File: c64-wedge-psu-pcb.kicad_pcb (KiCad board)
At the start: 2 copper layers, 70 x 54 mm, 16 parts, among them U1 LM2576T-5

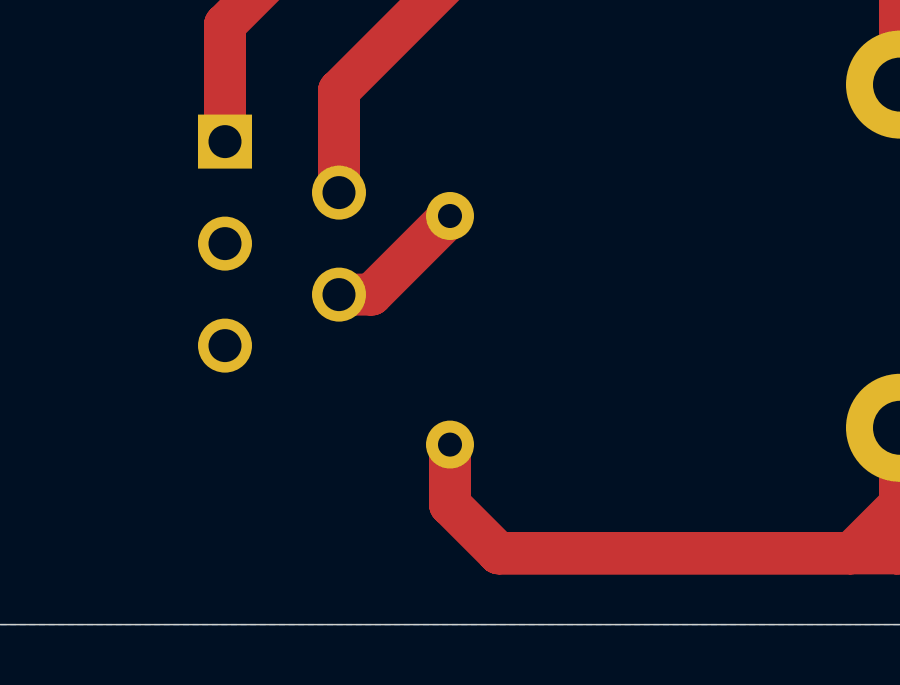
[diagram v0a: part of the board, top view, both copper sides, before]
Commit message: Make R1 pads bigger
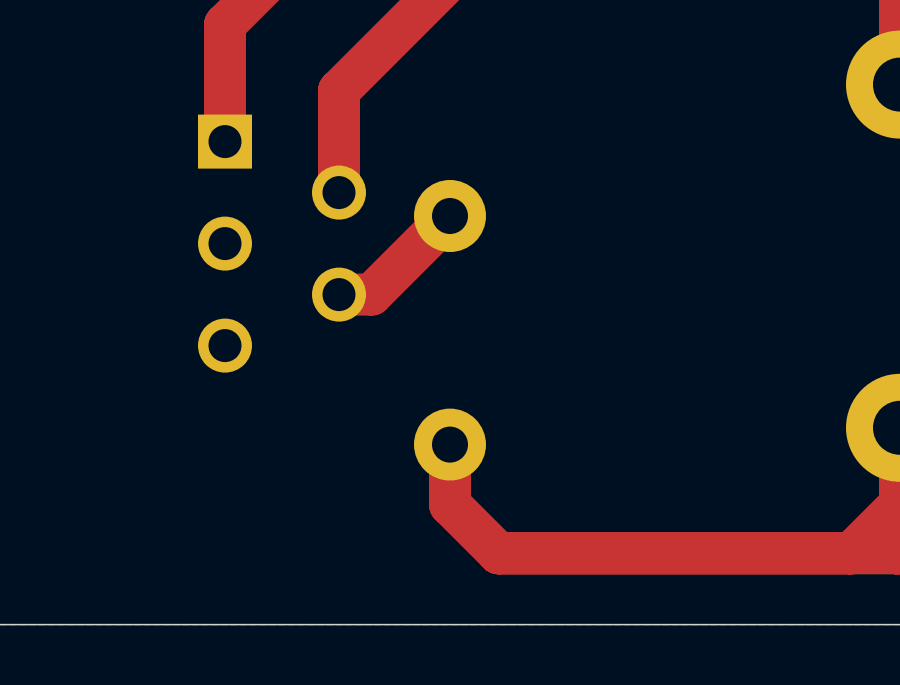
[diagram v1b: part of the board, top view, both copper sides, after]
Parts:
- R1: footprint Resistor_THT:R_Axial_DIN0207_L6.3mm_D2.5mm_P7.62mm_Horizontal -> Resistor_THT:R_Axial_DIN0411_L9.9mm_D3.6mm_P7.62mm_Vertical
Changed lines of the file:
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@@
     (add_net "Net-(R1-Pad2)")
+  )
+  (module Resistor_THT:R_Axial_DIN0411_L9.9mm_D3.6mm_P7.62mm_Vertical (layer B.Cu)
+    (at 117.5 108 90)
+    (descr "Resistor, Axial_DIN0411 series, Axial, Vertical, pin pitch=7.62mm, 1W, length*diameter=9.9*3.6mm^2")
+    (tags "Resistor Axial_DIN0411 series Axial Vertical pin pitch 7.62mm 1W length 9.9mm diameter 3.6mm")
+    (fp_text reference R1 (at 4 0 180) (layer B.SilkS)
+      (effects (font (size 1 1) (thickness 0.15)) (justify mirror))
+    )
+    (fp_text value 0R (at 3.81 -2.92 90) (layer B.Fab)
+      (effects (font (size 1 1) (thickness 0.15)) (justify mirror))
+    )
+    (fp_text user %R (at 3.81 2.92 90) (layer B.Fab)
+      (effects (font (size 1 1) (thickness 0.15)) (justify mirror))
+    )
+    (fp_line (start 9.07 2.05) (end -2.05 2.05) (layer B.CrtYd) (width 0.05))
+    (fp_line (start 9.07 -2.05) (end 9.07 2.05) (layer B.CrtYd) (width 0.05))
+    (fp_line (start -2.05 -2.05) (end 9.07 -2.05) (layer B.CrtYd) (width 0.05))
+    (fp_line (start -2.05 2.05) (end -2.05 -2.05) (layer B.CrtYd) (width 0.05))
+    (fp_line (start 1.92 0) (end 6.12 0) (layer B.SilkS) (width 0.12))
+    (fp_line (start 0 0) (end 7.62 0) (layer B.Fab) (width 0.1))
+    (fp_circle (center 0 0) (end 1.92 0) (layer B.SilkS) (width 0.12))
+    (fp_circle (center 0 0) (end 1.8 0) (layer B.Fab) (width 0.1))
+    (pad 2 thru_hole oval (at 7.62 0 90) (size 2.4 2.4) (drill 1.2) (layers *.Cu *.Mask)
+      (net 8 "Net-(R1-Pad2)"))
+    (pad 1 thru_hole circle (at 0 0 90) (size 2.4 2.4) (drill 1.2) (layers *.Cu *.Mask)
+      (net 2 "Net-(C2-Pad1)"))
+    (model ${KISYS3DMOD}/Resistor_THT.3dshapes/R_Axial_DIN0411_L9.9mm_D3.6mm_P7.62mm_Vertical.wrl
+      (at (xyz 0 0 0))
+      (scale (xyz 1 1 1))
+      (rotate (xyz 0 0 0))
+    )
   )
   (module Symbol:OSHW-Logo2_7.3x6mm_SilkScreen (layer F.Cu)
@@
       (effects (font (size 1 1) (thickness 0.15)) (justify mirror))
     )
-    (fp_text user K (at 0 2.6 90) (layer B.SilkS)
+    (fp_text user K (at 0 2.6 180) (layer B.SilkS)
       (effects (font (size 1 1) (thickness 0.15)) (justify mirror))
     )
@@
     )
   )
-  (module Resistor_THT:R_Axial_DIN0207_L6.3mm_D2.5mm_P7.62mm_Horizontal (layer B.Cu)
-    (at 117.5 108 90)
-    (descr "Resistor, Axial_DIN0207 series, Axial, Horizontal, pin pitch=7.62mm, 0.25W = 1/4W, length*diameter=6.3*2.5mm^2, http://cdn-reichelt.de/documents/datenblatt/B400/1_4W%23YAG.pdf")
-    (tags "Resistor Axial_DIN0207 series Axial Horizontal pin pitch 7.62mm 0.25W = 1/4W length 6.3mm diameter 2.5mm")
-    (fp_text reference R1 (at 3.81 0 180) (layer B.SilkS)
-      (effects (font (size 1 1) (thickness 0.15)) (justify mirror))
-    )
-    (fp_text value 0R (at 3.81 -2.37 90) (layer B.Fab)
-      (effects (font (size 1 1) (thickness 0.15)) (justify mirror))
-    )
-    (fp_line (start 0.66 1.25) (end 0.66 -1.25) (layer B.Fab) (width 0.1))
-    (fp_line (start 0.66 -1.25) (end 6.96 -1.25) (layer B.Fab) (width 0.1))
-    (fp_line (start 6.96 -1.25) (end 6.96 1.25) (layer B.Fab) (width 0.1))
-    (fp_line (start 6.96 1.25) (end 0.66 1.25) (layer B.Fab) (width 0.1))
-    (fp_line (start 0 0) (end 0.66 0) (layer B.Fab) (width 0.1))
-    (fp_line (start 7.62 0) (end 6.96 0) (layer B.Fab) (width 0.1))
-    (fp_line (start 0.54 1.04) (end 0.54 1.37) (layer B.SilkS) (width 0.12))
-    (fp_line (start 0.54 1.37) (end 7.08 1.37) (layer B.SilkS) (width 0.12))
-    (fp_line (start 7.08 1.37) (end 7.08 1.04) (layer B.SilkS) (width 0.12))
-    (fp_line (start 0.54 -1.04) (end 0.54 -1.37) (layer B.SilkS) (width 0.12))
-    (fp_line (start 0.54 -1.37) (end 7.08 -1.37) (layer B.SilkS) (width 0.12))
-    (fp_line (start 7.08 -1.37) (end 7.08 -1.04) (layer B.SilkS) (width 0.12))
-    (fp_line (start -1.05 1.5) (end -1.05 -1.5) (layer B.CrtYd) (width 0.05))
-    (fp_line (start -1.05 -1.5) (end 8.67 -1.5) (layer B.CrtYd) (width 0.05))
-    (fp_line (start 8.67 -1.5) (end 8.67 1.5) (layer B.CrtYd) (width 0.05))
-    (fp_line (start 8.67 1.5) (end -1.05 1.5) (layer B.CrtYd) (width 0.05))
-    (fp_text user %R (at 3.81 0 90) (layer B.Fab)
-      (effects (font (size 1 1) (thickness 0.15)) (justify mirror))
-    )
-    (pad 1 thru_hole circle (at 0 0 90) (size 1.6 1.6) (drill 0.8) (layers *.Cu *.Mask)
-      (net 2 "Net-(C2-Pad1)"))
-    (pad 2 thru_hole oval (at 7.62 0 90) (size 1.6 1.6) (drill 0.8) (layers *.Cu *.Mask)
-      (net 8 "Net-(R1-Pad2)"))
-    (model ${KISYS3DMOD}/Resistor_THT.3dshapes/R_Axial_DIN0207_L6.3mm_D2.5mm_P7.62mm_Horizontal.wrl
-      (at (xyz 0 0 0))
-      (scale (xyz 1 1 1))
-      (rotate (xyz 0 0 0))
-    )
-  )
   (module Connector_PinHeader_2.54mm:PinHeader_1x02_P2.54mm_Vertical (layer B.Cu)
     (at 152 80.5 270)
@@
   (segment (start 146 111) (end 145.37501 111.62499) (width 1.4) (layer F.Cu) (net 2))
   (segment (start 141 88) (end 146 93) (width 1.4) (layer F.Cu) (net 2))
-  (segment (start 117.5 110) (end 117.5 108) (width 1.4) (layer F.Cu) (net 2))
   (segment (start 130.860594 111.62499) (end 119.12499 111.62499) (width 1.4) (layer F.Cu) (net 2))
   (segment (start 132.5 107.44) (end 132.5 109.985584) (width 1.4) (layer F.Cu) (net 2))
@@
   (segment (start 146 100) (end 146 102) (width 1.4) (layer F.Cu) (net 2))
   (segment (start 146 102) (end 146 111) (width 1.4) (layer F.Cu) (net 2))
+  (segment (start 117.5 108) (end 117.5 110) (width 1.4) (layer F.Cu) (net 2))
   (segment (start 93.5 73.5) (end 93.5 77.6) (width 1.4) (layer F.Cu) (net 3))
   (segment (start 104 63) (end 93.5 73.5) (width 1.4) (layer F.Cu) (net 3))
@@
   (segment (start 142 63) (end 149 70) (width 1.4) (layer F.Cu) (net 7))
   (segment (start 149 70) (end 152 70) (width 1.4) (layer F.Cu) (net 7))
+  (segment (start 113.8 103) (end 114.88 103) (width 1.4) (layer F.Cu) (net 8))
   (segment (start 114.88 103) (end 117.5 100.38) (width 1.4) (layer F.Cu) (net 8))
-  (segment (start 113.8 103) (end 114.88 103) (width 1.4) (layer F.Cu) (net 8))
   (segment (start 152 79.12) (end 149.38 76.5) (width 1.4) (layer F.Cu) (net 9))
   (segment (start 152 80.5) (end 152 79.12) (width 1.4) (layer F.Cu) (net 9))

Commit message: relayout, change some values and footprints
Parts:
- C1, C2: footprint Capacitor_THT:CP_Radial_D18.0mm_P7.50mm -> Capacitor_THT:CP_Radial_D16.0mm_P7.50mm
- C3: footprint Capacitor_THT:CP_Radial_D6.3mm_P2.50mm -> Capacitor_THT:CP_Radial_D8.0mm_P3.50mm
- L2: renamed from L3; value 22uH -> 20uH; footprint Inductor_THT:L_Toroid_Vertical_L19.1mm_W8.1mm_P7.10mm_Bourns_5700 -> Inductor_THT:L_Toroid_Vertical_L16.0mm_W8.0mm_P7.62mm
- R1: footprint Resistor_THT:R_Axial_DIN0411_L9.9mm_D3.6mm_P7.62mm_Vertical -> Resistor_THT:R_Axial_DIN0411_L9.9mm_D3.6mm_P5.08mm_Vertical
- U1: footprint Package_TO_SOT_THT:TO-220-5_P3.4x3.8mm_StaggerEven_Lead7.13mm_TabDown -> Package_TO_SOT_THT:TO-220-5_P3.4x3.7mm_StaggerEven_Lead3.8mm_Vertical
- moved R1 15.3 mm to (132.5, 111.0), turned to 180 degrees
- moved U1 2.56 mm to (112.5, 97.3)
- moved C1 1.12 mm to (115.5, 87.0)
- moved C2 1.00 mm to (141.0, 87.0)
- moved L1 1.00 mm to (132.5, 95.0)
- moved C3 0.90 mm to (156.5, 86.8)
- moved D2 0.50 mm to (128.5, 89.5)
- moved L2 0.50 mm to (148.5, 101.0)
- renumbered L2 to L1
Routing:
- net Net-(C2-Pad1): track 92.8 -> 52.5 mm
- net Net-(R1-Pad2): track 4.79 -> 18.1 mm
- net Net-(D2-Pad1): track 29.2 -> 27.1 mm

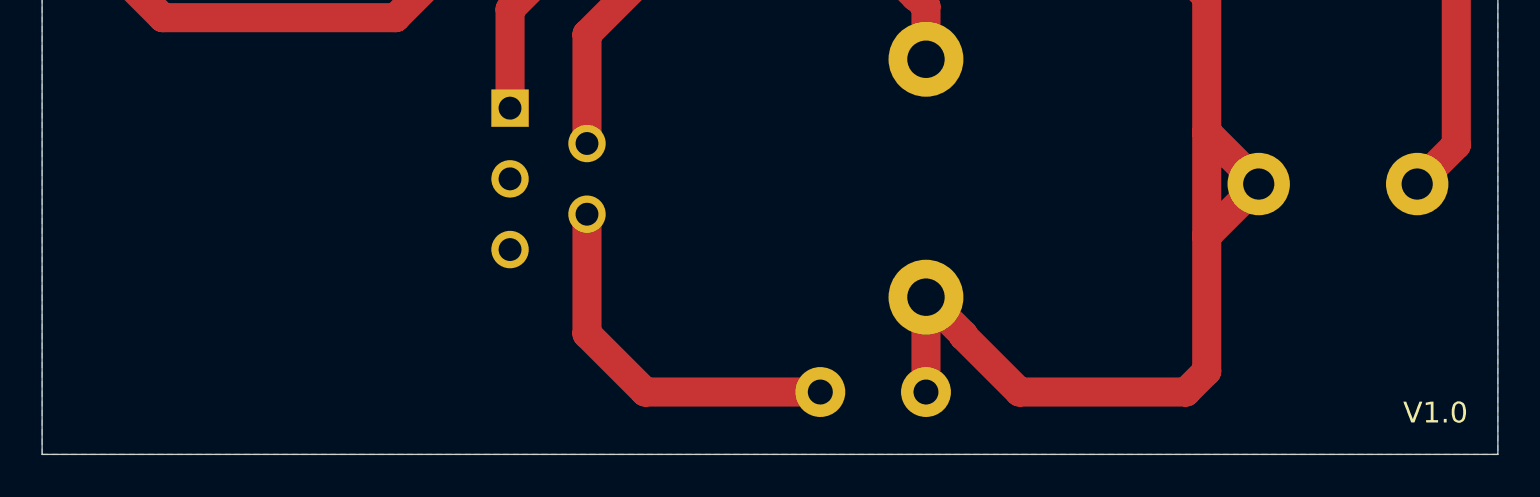
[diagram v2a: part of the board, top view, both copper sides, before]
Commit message: Modify footprints, add some info text, modify resistor values
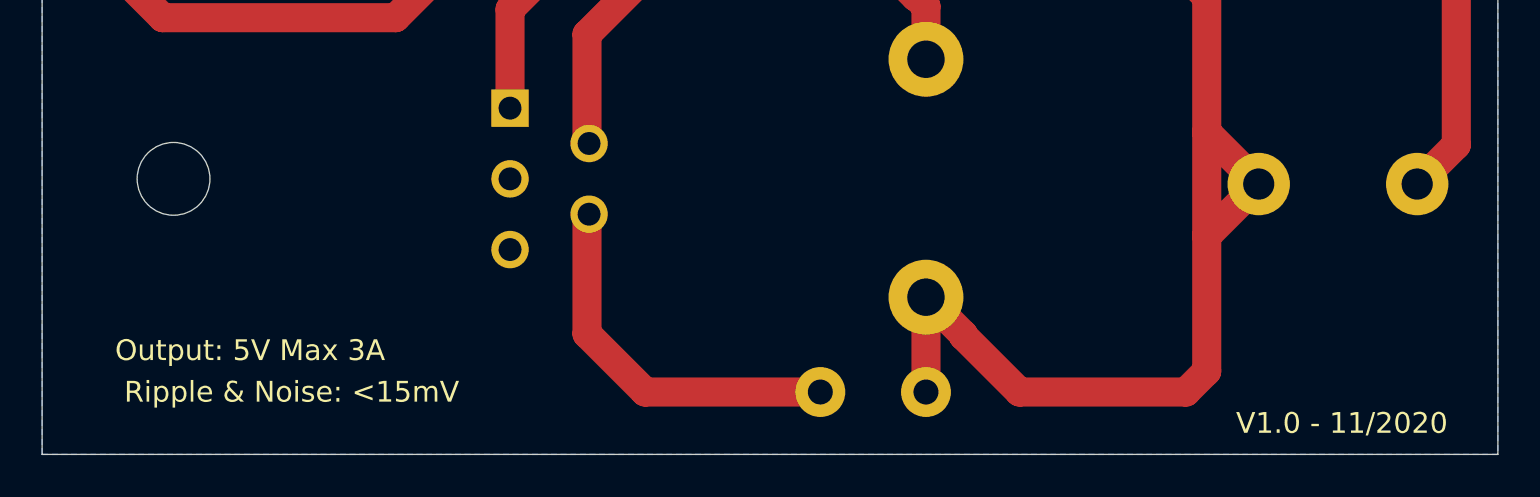
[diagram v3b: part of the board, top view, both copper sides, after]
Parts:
- C3: value 100uF -> 220uF 50V
- R1: value 0R -> 200R
- R2: value 330R -> 200R
- U1: footprint Package_TO_SOT_THT:TO-220-5_P3.4x3.7mm_StaggerEven_Lead3.8mm_Vertical -> Package_TO_SOT_THT:TO-220-5_P3.4x3.8mm_StaggerEven_Lead7.13mm_TabDown
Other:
- board text added: "Output: 5V Max 3A"
- board text added: "Ripple & Noise: <15mV"
- board text added: "V1.0 - 11/2020"
- board text removed: "V1.0"

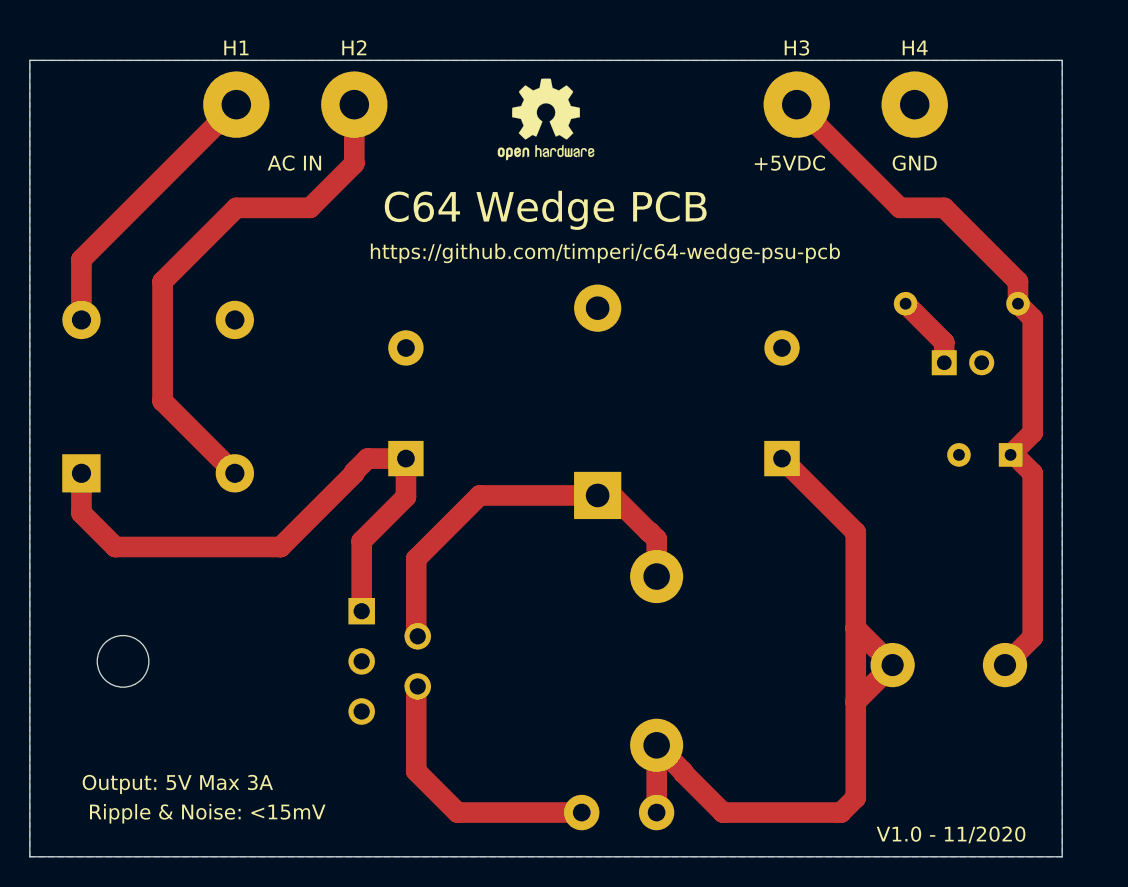
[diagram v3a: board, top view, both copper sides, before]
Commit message: V1.1: Proper voltage divider to Feedback line. Make tracks wider. Some relayout. Update resistor values and L2 value.
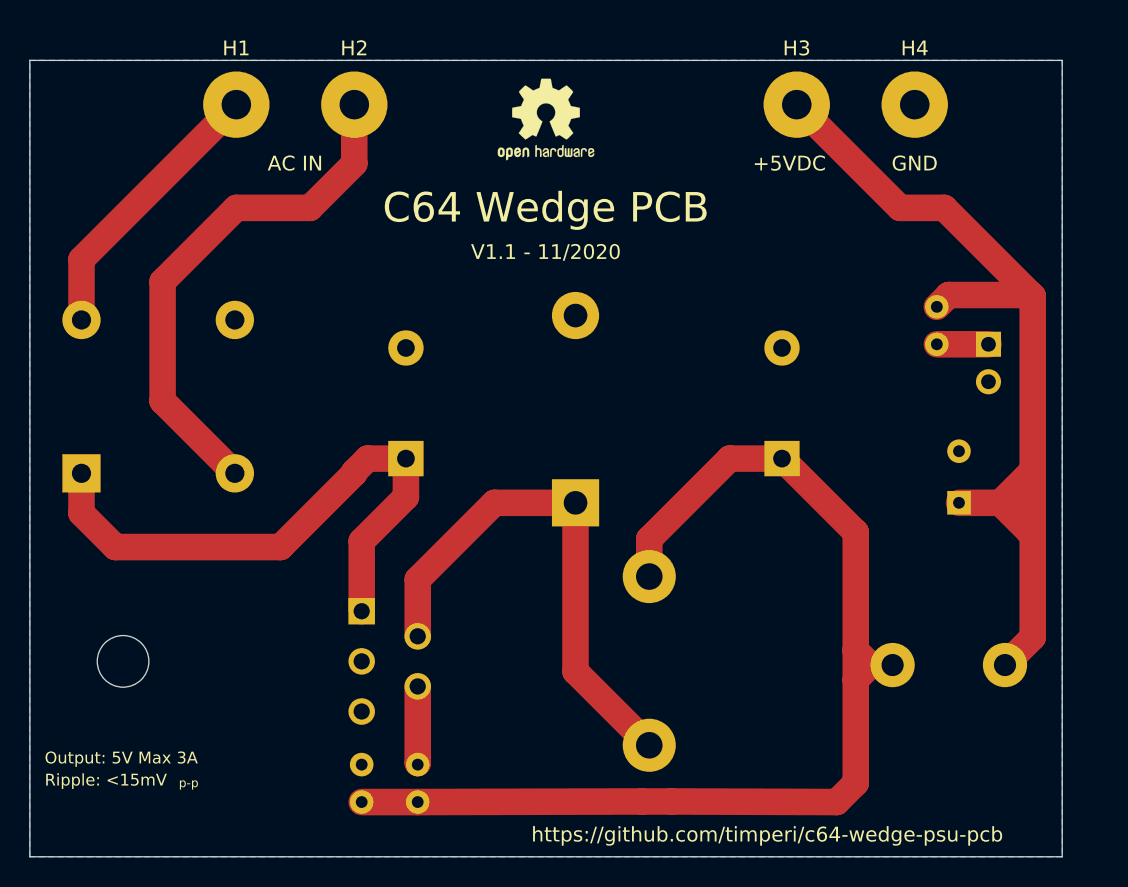
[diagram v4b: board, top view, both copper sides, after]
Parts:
- added R3: 5000R, Resistor_THT:R_Axial_DIN0207_L6.3mm_D2.5mm_P2.54mm_Vertical, B.Cu at (112.5, 107.8)
- D2: value 550mV 5A -> 5A
- L2: value 20uH -> 22uH
- R1: footprint Resistor_THT:R_Axial_DIN0411_L9.9mm_D3.6mm_P5.08mm_Vertical -> Resistor_THT:R_Axial_DIN0207_L6.3mm_D2.5mm_P2.54mm_Vertical
- R2: footprint Resistor_THT:R_Axial_DIN0207_L6.3mm_D2.5mm_P7.62mm_Horizontal -> Resistor_THT:R_Axial_DIN0207_L6.3mm_D2.5mm_P2.54mm_Vertical
- moved R1 16.5 mm to (116.3, 107.8), turned to 270 degrees
- moved L1 11.5 mm to (132.0, 106.4), turned to 0 degrees
- moved R2 5.50 mm to (151.5, 76.7), turned to 270 degrees
- moved C3 4.78 mm to (153.0, 90.0), turned to 90 degrees
- moved LED1 3.25 mm to (155.0, 79.2), turned to 180 degrees
- moved D2 1.58 mm to (127.0, 90.0)
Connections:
- R1 pad 1: Net-(C2-Pad1) -> Net-(R1-Pad1)
- R1 pad 2: Net-(R1-Pad2) -> Net-(C2-Pad1)
- U1 pad 4: Net-(R1-Pad2) -> Net-(R1-Pad1)
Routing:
- net Net-(C2-Pad1): track 52.5 -> 76.2 mm
- net Net-(R1-Pad2): track 18.1 -> 0.00 mm
- net /+5VDC: track 50.1 -> 64.5 mm
- net Net-(D2-Pad1): track 27.1 -> 35.3 mm
- net Net-(R1-Pad1): track 0.00 -> 5.19 mm
- net Net-(LED1-Pad1): track 5.09 -> 3.50 mm
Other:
- net class Default: trace_width 1.4 -> 1.8
- board text added: "Ripple: <15mV"
- board text added: "V1.1 - 11/2020"
- board text added: "p-p"
- board text removed: "Ripple & Noise: <15mV"
- board text removed: "V1.0 - 11/2020"

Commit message: update resistor values
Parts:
- C3: value 220uF 50V -> 220uF
- R3: value 5000R -> 4700R
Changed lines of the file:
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@@
       (effects (font (size 1 1) (thickness 0.15)) (justify mirror))
     )
-    (fp_text value 5000R (at 1.27 -2.37 270) (layer B.Fab)
+    (fp_text value 4700R (at 1.27 -2.37 270) (layer B.Fab)
       (effects (font (size 1 1) (thickness 0.15)) (justify mirror))
     )
@@
       (effects (font (size 1 1) (thickness 0.15)) (justify mirror))
     )
-    (fp_text value "220uF 50V" (at 1.75 -5.25 90) (layer B.Fab)
+    (fp_text value 220uF (at 1.75 -5.25 90) (layer B.Fab)
       (effects (font (size 1 1) (thickness 0.15)) (justify mirror))
     )
@@
   (segment (start 115.5 89.6) (end 112.5 92.6) (width 1.8) (layer F.Cu) (net 1))
   (segment (start 146 92) (end 141 87) (width 1.8) (layer F.Cu) (net 2) (status 20))
-  (segment (start 132.5 106.44) (end 132.5 106.5) (width 1.8) (layer F.Cu) (net 5) (status 30))
   (segment (start 116.3 110.29) (end 112.5 110.29) (width 1.8) (layer F.Cu) (net 2) (status 30))
   (segment (start 116.3 110.29) (end 131.5 110.25) (width 1.8) (layer F.Cu) (net 2) (status 10))
@@
   (segment (start 104 70) (end 99 75) (width 1.8) (layer F.Cu) (net 4))
   (segment (start 109 70) (end 104 70) (width 1.8) (layer F.Cu) (net 4))
+  (segment (start 132.5 106.44) (end 132.5 106.5) (width 1.8) (layer F.Cu) (net 5) (status 30))
   (segment (start 116.3 99.05) (end 116.3 95.2) (width 1.8) (layer F.Cu) (net 5) (status 10))
   (segment (start 116.3 95.2) (end 121.5 90) (width 1.8) (layer F.Cu) (net 5))
